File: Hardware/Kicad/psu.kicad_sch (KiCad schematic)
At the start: 21 parts, among them J7 Barrel_Jack_Switch, U7 TPS62160DSG, U8 TPS7A2033PDBVR, U9 TPS7A2018PDBVR

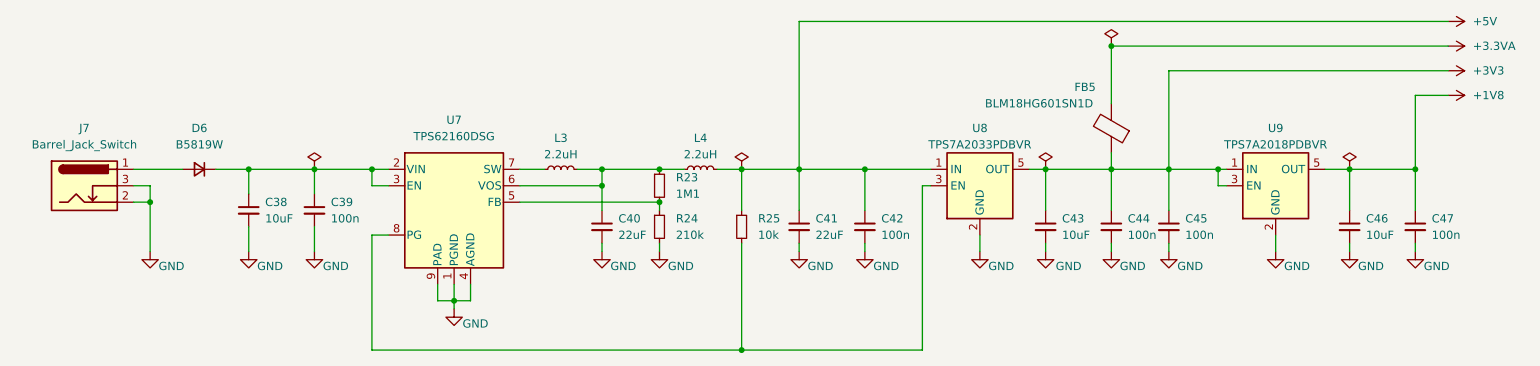
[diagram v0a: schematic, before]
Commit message: Update with ML2032 battery
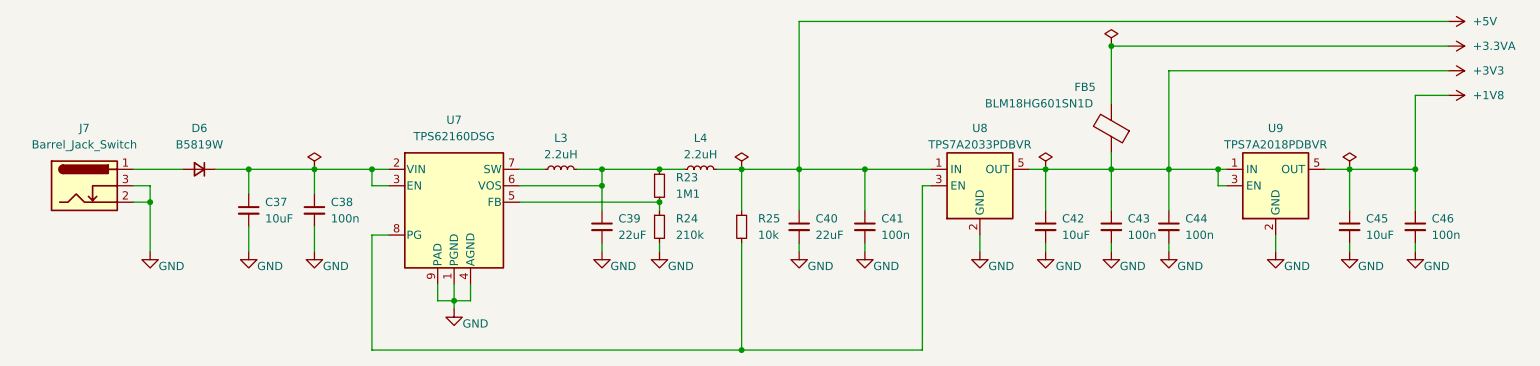
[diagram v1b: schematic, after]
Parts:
- renumbered C38 to C37, C39 to C38, C40 to C39, C41 to C40, C42 to C41, C43 to C42, C44 to C43, C45 to C44, C46 to C45, C47 to C46
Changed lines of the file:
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@@
 		(dnp no)
 		(fields_autoplaced yes)
-		(property "Reference" "C41"
+		(property "Reference" "C40"
 			(at 148.59 53.3462 0)
 			(show_name no)
@@
 			(project "PAL-sign"
 				(path "/5e4b4b86-505e-4573-b1db-0e4430e7f8ee"
-					(reference "C41")
+					(reference "C40")
 					(unit 1)
 				)
@@
 		(dnp no)
 		(fields_autoplaced yes)
-		(property "Reference" "C45"
+		(property "Reference" "C44"
 			(at 205.74 53.3462 0)
 			(show_name no)
@@
 			(project "PAL-sign"
 				(path "/5e4b4b86-505e-4573-b1db-0e4430e7f8ee"
-					(reference "C45")
+					(reference "C44")
 					(unit 1)
 				)
@@
 		(dnp no)
 		(fields_autoplaced yes)
-		(property "Reference" "C47"
+		(property "Reference" "C46"
 			(at 243.84 53.3462 0)
 			(show_name no)
@@
 			(project "PAL-sign"
 				(path "/5e4b4b86-505e-4573-b1db-0e4430e7f8ee"
-					(reference "C47")
+					(reference "C46")
 					(unit 1)
 				)
@@
 		(dnp no)
 		(fields_autoplaced yes)
-		(property "Reference" "C44"
+		(property "Reference" "C43"
 			(at 196.85 53.3462 0)
 			(show_name no)
@@
 			(project "PAL-sign"
 				(path "/5e4b4b86-505e-4573-b1db-0e4430e7f8ee"
-					(reference "C44")
+					(reference "C43")
 					(unit 1)
 				)
@@
 		(dnp no)
 		(fields_autoplaced yes)
-		(property "Reference" "C43"
+		(property "Reference" "C42"
 			(at 186.69 53.3462 0)
 			(show_name no)
@@
 			(project "PAL-sign"
 				(path "/5e4b4b86-505e-4573-b1db-0e4430e7f8ee"
-					(reference "C43")
+					(reference "C42")
 					(unit 1)
 				)
@@
 		(dnp no)
 		(fields_autoplaced yes)
-		(property "Reference" "C42"
+		(property "Reference" "C41"
 			(at 158.75 53.3462 0)
 			(show_name no)
@@
 			(project "PAL-sign"
 				(path "/5e4b4b86-505e-4573-b1db-0e4430e7f8ee"
-					(reference "C42")
+					(reference "C41")
 					(unit 1)
 				)
@@
 		(dnp no)
 		(fields_autoplaced yes)
-		(property "Reference" "C46"
+		(property "Reference" "C45"
 			(at 233.68 53.3462 0)
 			(show_name no)
@@
 			(project "PAL-sign"
 				(path "/5e4b4b86-505e-4573-b1db-0e4430e7f8ee"
-					(reference "C46")
+					(reference "C45")
 					(unit 1)
 				)
@@
 		(dnp no)
 		(fields_autoplaced yes)
-		(property "Reference" "C38"
+		(property "Reference" "C37"
 			(at 63.5 50.8062 0)
 			(show_name no)
@@
 			(project "PAL-sign"
 				(path "/5e4b4b86-505e-4573-b1db-0e4430e7f8ee"
-					(reference "C38")
+					(reference "C37")
 					(unit 1)
 				)
@@
 		(dnp no)
 		(fields_autoplaced yes)
-		(property "Reference" "C39"
+		(property "Reference" "C38"
 			(at 73.66 50.8062 0)
 			(show_name no)
@@
 			(project "PAL-sign"
 				(path "/5e4b4b86-505e-4573-b1db-0e4430e7f8ee"
-					(reference "C39")
+					(reference "C38")
 					(unit 1)
 				)
@@
 		(dnp no)
 		(fields_autoplaced yes)
-		(property "Reference" "C40"
+		(property "Reference" "C39"
 			(at 118.11 53.3462 0)
 			(show_name no)
@@
 			(project "PAL-sign"
 				(path "/5e4b4b86-505e-4573-b1db-0e4430e7f8ee"
-					(reference "C40")
+					(reference "C39")
 					(unit 1)
 				)

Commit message: Small hardware update
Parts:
- renumbered C37 to C38, C38 to C39, C39 to C40, C40 to C41, C41 to C42, C42 to C43, C43 to C44, C44 to C45, C45 to C46, C46 to C47
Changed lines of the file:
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@@
 		(dnp no)
 		(fields_autoplaced yes)
-		(property "Reference" "C40"
+		(property "Reference" "C41"
 			(at 148.59 53.3462 0)
 			(show_name no)
@@
 			(project "PAL-sign"
 				(path "/5e4b4b86-505e-4573-b1db-0e4430e7f8ee"
-					(reference "C40")
+					(reference "C41")
 					(unit 1)
 				)
@@
 		(dnp no)
 		(fields_autoplaced yes)
-		(property "Reference" "C44"
+		(property "Reference" "C45"
 			(at 205.74 53.3462 0)
 			(show_name no)
@@
 			(project "PAL-sign"
 				(path "/5e4b4b86-505e-4573-b1db-0e4430e7f8ee"
-					(reference "C44")
+					(reference "C45")
 					(unit 1)
 				)
@@
 		(dnp no)
 		(fields_autoplaced yes)
-		(property "Reference" "C46"
+		(property "Reference" "C47"
 			(at 243.84 53.3462 0)
 			(show_name no)
@@
 			(project "PAL-sign"
 				(path "/5e4b4b86-505e-4573-b1db-0e4430e7f8ee"
-					(reference "C46")
+					(reference "C47")
 					(unit 1)
 				)
@@
 		(dnp no)
 		(fields_autoplaced yes)
-		(property "Reference" "C43"
+		(property "Reference" "C44"
 			(at 196.85 53.3462 0)
 			(show_name no)
@@
 			(project "PAL-sign"
 				(path "/5e4b4b86-505e-4573-b1db-0e4430e7f8ee"
-					(reference "C43")
+					(reference "C44")
 					(unit 1)
 				)
@@
 		(dnp no)
 		(fields_autoplaced yes)
-		(property "Reference" "C42"
+		(property "Reference" "C43"
 			(at 186.69 53.3462 0)
 			(show_name no)
@@
 			(project "PAL-sign"
 				(path "/5e4b4b86-505e-4573-b1db-0e4430e7f8ee"
-					(reference "C42")
+					(reference "C43")
 					(unit 1)
 				)
@@
 		(dnp no)
 		(fields_autoplaced yes)
-		(property "Reference" "C41"
+		(property "Reference" "C42"
 			(at 158.75 53.3462 0)
 			(show_name no)
@@
 			(project "PAL-sign"
 				(path "/5e4b4b86-505e-4573-b1db-0e4430e7f8ee"
-					(reference "C41")
+					(reference "C42")
 					(unit 1)
 				)
@@
 		(dnp no)
 		(fields_autoplaced yes)
-		(property "Reference" "C45"
+		(property "Reference" "C46"
 			(at 233.68 53.3462 0)
 			(show_name no)
@@
 			(project "PAL-sign"
 				(path "/5e4b4b86-505e-4573-b1db-0e4430e7f8ee"
-					(reference "C45")
+					(reference "C46")
 					(unit 1)
 				)
@@
 		(dnp no)
 		(fields_autoplaced yes)
-		(property "Reference" "C37"
+		(property "Reference" "C38"
 			(at 63.5 50.8062 0)
 			(show_name no)
@@
 			(project "PAL-sign"
 				(path "/5e4b4b86-505e-4573-b1db-0e4430e7f8ee"
-					(reference "C37")
+					(reference "C38")
 					(unit 1)
 				)
@@
 		(dnp no)
 		(fields_autoplaced yes)
-		(property "Reference" "C38"
+		(property "Reference" "C39"
 			(at 73.66 50.8062 0)
 			(show_name no)
@@
 			(project "PAL-sign"
 				(path "/5e4b4b86-505e-4573-b1db-0e4430e7f8ee"
-					(reference "C38")
+					(reference "C39")
 					(unit 1)
 				)
@@
 		(dnp no)
 		(fields_autoplaced yes)
-		(property "Reference" "C39"
+		(property "Reference" "C40"
 			(at 118.11 53.3462 0)
 			(show_name no)
@@
 			(project "PAL-sign"
 				(path "/5e4b4b86-505e-4573-b1db-0e4430e7f8ee"
-					(reference "C39")
+					(reference "C40")
 					(unit 1)
 				)
